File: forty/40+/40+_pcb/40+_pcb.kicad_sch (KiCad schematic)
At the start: 28 parts, among them J1 USB_C_Receptacle_USB2.0_16P, J2 Conn_01x02_Socket, SW1 Switch, U1 USB6B1, U2 USBLC6-2SC6, U3 nRF52840, U4 MCP73831-2-OT, Y2 Crystal_GND3

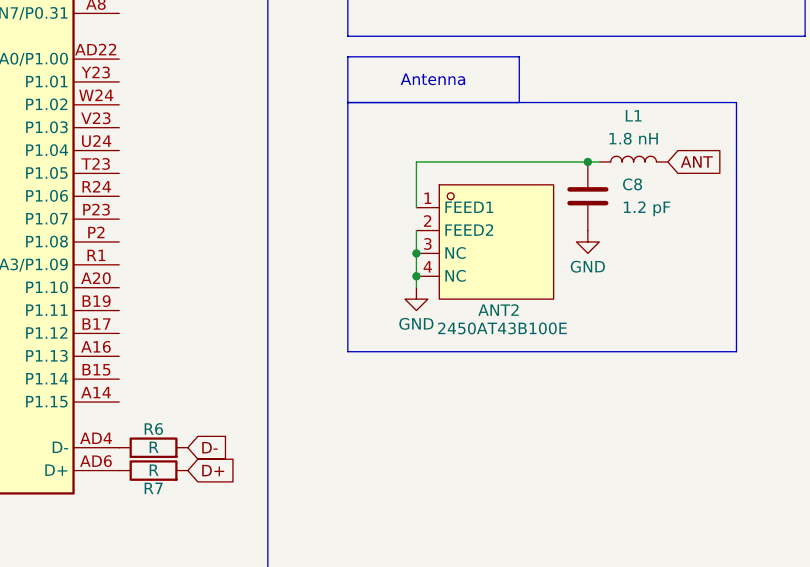
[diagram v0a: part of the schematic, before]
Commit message: Add EasyEDA to KiCad symbol and 3D models
Added EasyEDA to KiCad symbol library and associated 3D STEP/WRL models for capacitor and resistor. Updated 40+ PCB project files, removed autosave and lock files, and added a backup ZIP.
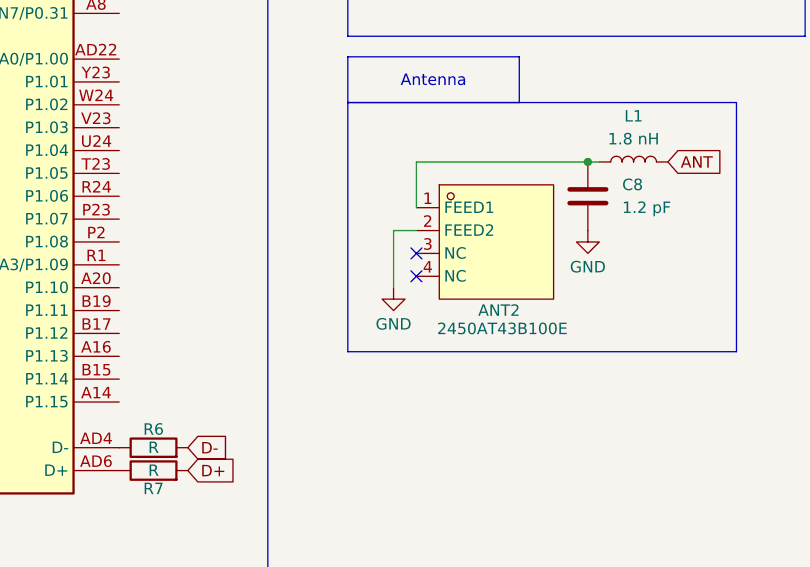
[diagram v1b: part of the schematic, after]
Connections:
- net GND: no longer ANT2.3 (NC), ANT2.4 (NC)
- no-connect marks 3 -> 5
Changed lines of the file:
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@@
-	)
-	(junction
-		(at 139.7 152.4)
-		(diameter 0)
-		(color 0 0 0 0)
 	)
 	(junction
@@
 	)
 	(junction
-		(at 139.7 154.94)
-		(diameter 0)
-		(color 0 0 0 0)
-	)
-	(junction
 		(at 213.36 142.24)
 		(diameter 0)
@@
 	)
 	(no_connect
+		(at 139.7 152.4)
+	)
+	(no_connect
 		(at 144.78 119.38)
+	)
+	(no_connect
+		(at 139.7 154.94)
 	)
 	(no_connect
@@
 	(wire
 		(pts
-			(xy 139.7 149.86) (xy 139.7 152.4)
-		)
-		(stroke
-			(width 0)
-			(type default)
-		)
-	)
-	(wire
-		(pts
 			(xy 223.52 127) (xy 231.14 127)
 		)
@@
 	(wire
 		(pts
+			(xy 137.16 149.86) (xy 139.7 149.86)
+		)
+		(stroke
+			(width 0)
+			(type default)
+		)
+	)
+	(wire
+		(pts
 			(xy 55.88 34.29) (xy 58.42 34.29)
 		)
@@
 	(wire
 		(pts
-			(xy 139.7 152.4) (xy 139.7 154.94)
-		)
-		(stroke
-			(width 0)
-			(type default)
-		)
-	)
-	(wire
-		(pts
 			(xy 38.1 153.67) (xy 38.1 156.21)
 		)
@@
 	(wire
 		(pts
-			(xy 139.7 154.94) (xy 139.7 156.21)
+			(xy 137.16 149.86) (xy 137.16 156.21)
 		)
 		(stroke
@@
 	(symbol
 		(lib_id "power:GND")
-		(at 139.7 156.21 0)
+		(at 137.16 156.21 0)
 		(unit 1)
 		(exclude_from_sim no)
@@
 		(dnp no)
 		(property "Reference" "#PWR019"
-			(at 139.7 162.56 0)
+			(at 137.16 162.56 0)
 			(effects
 				(font
@@
 		)
 		(property "Value" "GND"
-			(at 139.7 160.274 0)
+			(at 137.16 160.274 0)
 			(effects
 				(font
@@
 		)
 		(property "Footprint" ""
-			(at 139.7 156.21 0)
+			(at 137.16 156.21 0)
 			(effects
 				(font
@@
 		)
 		(property "Datasheet" ""
-			(at 139.7 156.21 0)
+			(at 137.16 156.21 0)
 			(effects
 				(font
@@
 		)
 		(property "Description" "Power symbol creates a global label with name \"GND\" , ground"
-			(at 139.7 156.21 0)
-			(effects
-				(font
+			(at 137.16 156.21 0)
+			(effects
+				(font

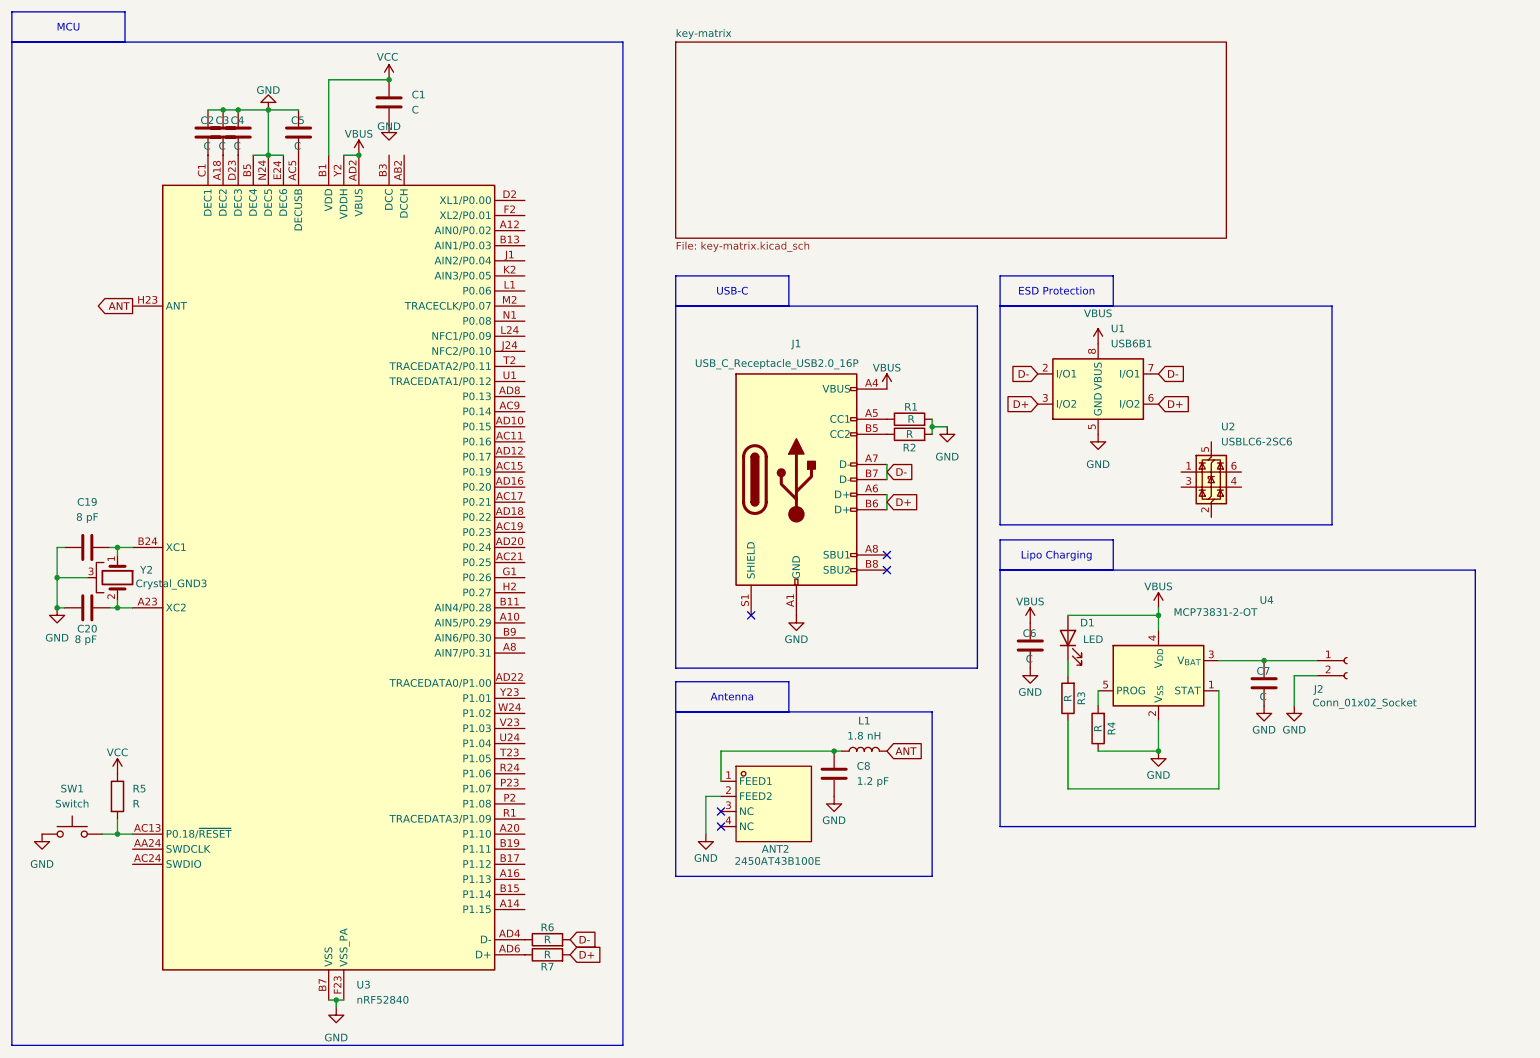
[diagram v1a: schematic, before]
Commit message: Add 40%+ keyboard layout and update PCB files
Added a new 40%+ keyboard layout JSON with function keys, updated and added KiCad PCB, schematic, and project files for the 40+ PCB, and included new backup and log files. Also added the nRF52840 spec sheet and made changes to the macropad PCB project file.
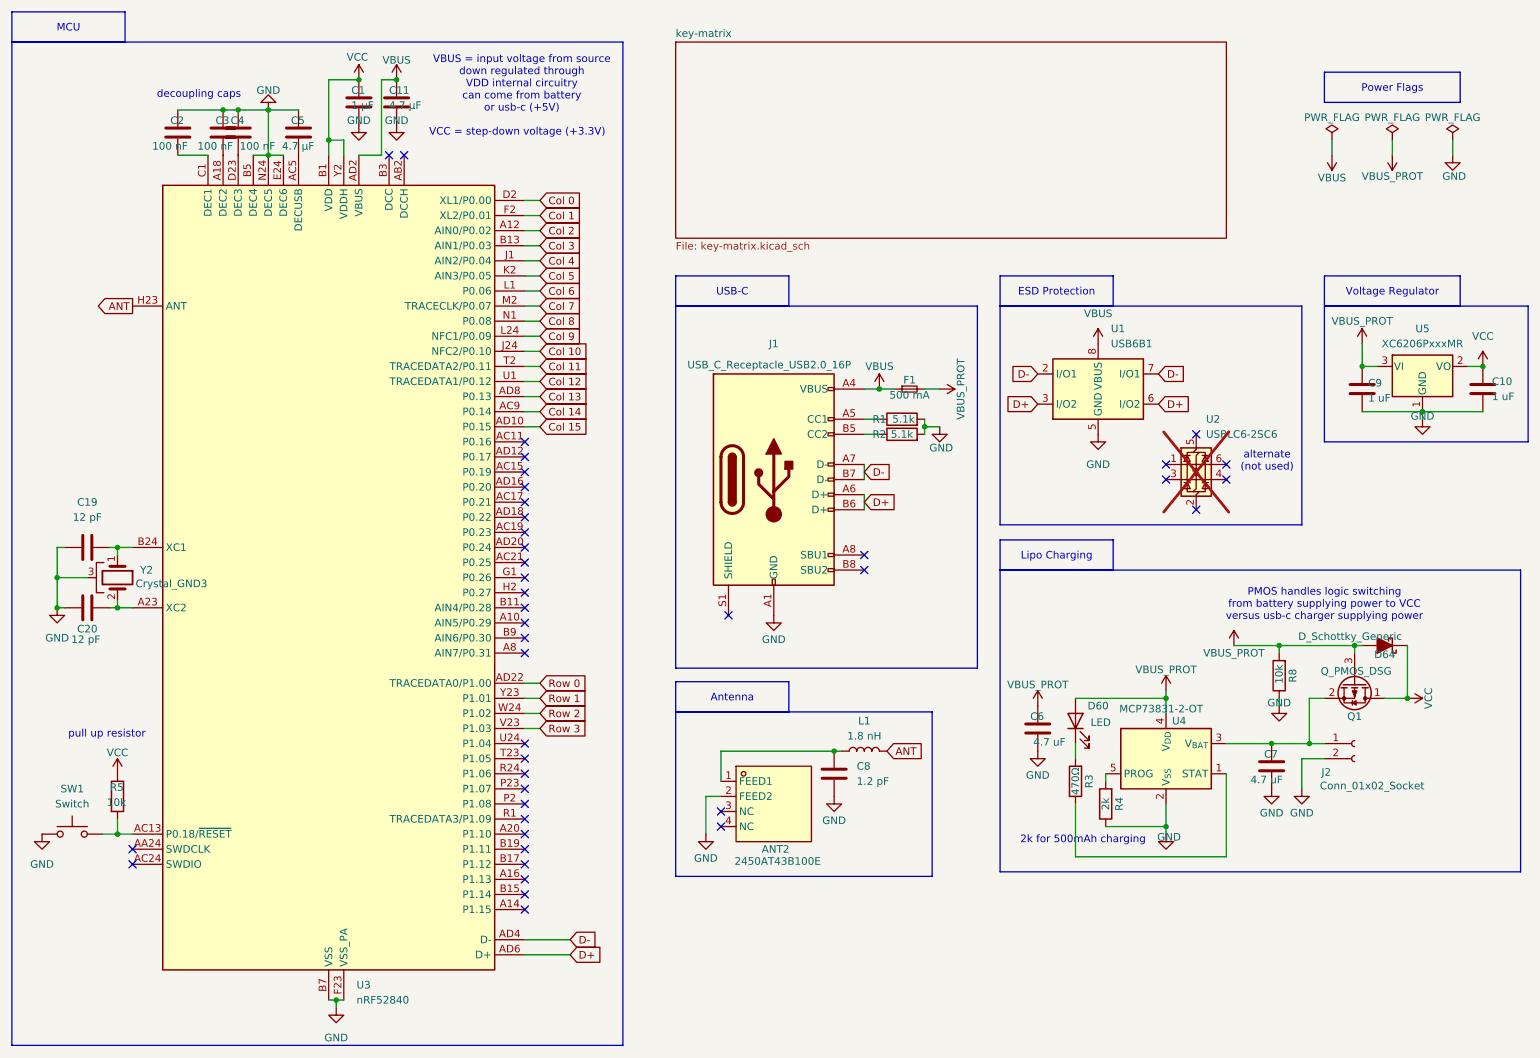
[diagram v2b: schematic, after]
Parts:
- removed R6, R7: R, symbol Device:R
- added C10, C9: 1 uF, Capacitor_SMD:C_0603_1608Metric_Pad1.08x0.95mm_HandSolder, symbol Device:C
- added C11: 4.7 µF, Capacitor_SMD:C_0603_1608Metric_Pad1.08x0.95mm_HandSolder, symbol Device:C
- added D64: D_Schottky_Generic, Diode_SMD:D_2114_3652Metric_Pad1.85x3.75mm_HandSolder, symbol PCM_Diode_Schottky_AKL:D_Schottky_Generic
- added F1: 500 mA, Fuse:Fuse_1206_3216Metric_Pad1.42x1.75mm_HandSolder, symbol Device:Fuse_Small
- added Q1: Q_PMOS_DSG, Package_TO_SOT_SMD:SOT-23, symbol Transistor_FET:Q_PMOS_DSG
- added R8: 10k, Resistor_SMD:R_0603_1608Metric_Pad0.98x0.95mm_HandSolder, symbol Device:R
- added U5: XC6206PxxxMR, Package_TO_SOT_SMD:SOT-23-3, symbol Regulator_Linear:XC6206PxxxMR
- C1: value C -> 1 µF; footprint (none) -> Capacitor_SMD:C_0603_1608Metric_Pad1.08x0.95mm_HandSolder
- C19, C20: value 8 pF -> 12 pF; footprint (none) -> Capacitor_SMD:C_0402_1005Metric_Pad0.74x0.62mm_HandSolder
- C2, C3, C4: value C -> 100 nF; footprint (none) -> Capacitor_SMD:C_0603_1608Metric_Pad1.08x0.95mm_HandSolder
- C5: value C -> 4.7 µF; footprint (none) -> Capacitor_SMD:C_0603_1608Metric_Pad1.08x0.95mm_HandSolder
- C6, C7: value C -> 4.7 uF; footprint (none) -> Capacitor_SMD:C_0603_1608Metric_Pad1.08x0.95mm_HandSolder
- C8: footprint (none) -> Capacitor_SMD:C_0402_1005Metric_Pad0.74x0.62mm_HandSolder
- D60: renamed from D1; footprint (none) -> LED_SMD:LED_0603_1608Metric_Pad1.05x0.95mm_HandSolder
- J1: footprint (none) -> Connector_USB:USB_C_Receptacle_HRO_TYPE-C-31-M-12
- J2: footprint (none) -> Connector_JST:JST_PH_S2B-PH-K_1x02_P2.00mm_Horizontal
- L1: footprint (none) -> Inductor_SMD:L_0402_1005Metric_Pad0.77x0.64mm_HandSolder
- R1, R2: value R -> 5.1k; footprint (none) -> Resistor_SMD:R_0603_1608Metric_Pad0.98x0.95mm_HandSolder
- R3: value R -> 470Ω; footprint (none) -> Resistor_SMD:R_0603_1608Metric_Pad0.98x0.95mm_HandSolder
- R4: value R -> 2k; footprint (none) -> Resistor_SMD:R_0603_1608Metric_Pad0.98x0.95mm_HandSolder
- R5: value R -> 10k; footprint (none) -> Resistor_SMD:R_0603_1608Metric_Pad0.98x0.95mm_HandSolder
- SW1: footprint Connector_JST:JST_EH_B2B-EH-A_1x02_P2.50mm_Vertical -> Button_Switch_SMD:SW_SPST_TL3342
- U2: now not fitted
- U4: footprint Package_TO_SOT_SMD:SOT-23-5 -> Package_TO_SOT_SMD:SOT-23-5_HandSoldering
- Y2: footprint (none) -> Crystal:Crystal_SMD_3225-4Pin_3.2x2.5mm_HandSoldering
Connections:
- net D+: now also U3.AD6 (D+)
- net D-: now also U3.AD4 (D-)
- net GND: now also C10.2, C11.2, C9.2, R8.1, U5.1 (GND)
- net VBUS: now also C11.1, F1.1; no longer C6.1, D60.2 (A), U3.Y2 (VDDH), U4.4 (V_{DD})
- net VCC: now also U3.Y2 (VDDH), C10.1, D64.1 (K), Q1.1 (D), U5.2 (VO)
- net at C7.1, J2.1 (Pin_1), U4.3 (V_{BAT}): now also Q1.2 (S)
- net Col 2: now reaches U3.A12 (AIN0/P0.02)
- net Col 14: now reaches U3.AC9 (P0.14)
- net Col 15: now reaches U3.AD10 (P0.15)
- net Row 0: now reaches U3.AD22 (TRACEDATA0/P1.00)
- net Col 13: now reaches U3.AD8 (P0.13)
- net Col 3: now reaches U3.B13 (AIN1/P0.03)
- net Col 0: now reaches U3.D2 (XL1/P0.00)
- net Col 1: now reaches U3.F2 (XL2/P0.01)
- net Col 4: now reaches U3.J1 (AIN2/P0.04)
- net Col 10: now reaches U3.J24 (NFC2/P0.10)
- net Col 5: now reaches U3.K2 (AIN3/P0.05)
- net Col 6: now reaches U3.L1 (P0.06)
- net Col 9: now reaches U3.L24 (NFC1/P0.09)
- net Col 7: now reaches U3.M2 (TRACECLK/P0.07)
- net Col 8: now reaches U3.N1 (P0.08)
- net Col 11: now reaches U3.T2 (TRACEDATA2/P0.11)
- net Col 12: now reaches U3.U1 (TRACEDATA1/P0.12)
- net Row 3: now reaches U3.V23 (P1.03)
- net Row 2: now reaches U3.W24 (P1.02)
- net Row 1: now reaches U3.Y23 (P1.01)
- new net VBUS_PROT: C6.1, C9.1, D60.2 (A), D64.2 (A), F1.2, Q1.3 (G), R8.2, U4.4 (V_{DD}), U5.3 (VI)
- no-connect marks 5 -> 42
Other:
- note added: "2k for 500mAh charging"
- note added: "PMOS handles logic switching from battery supplying power to VCC versus usb-c charger supplying power"
- note added: "VBUS = input voltage from source down regulated through VDD internal circuitry can come from battery or usb-c (+5V)"
- note added: "VCC = step-down voltage (+3.3V)"
- note added: "alternate (not used)"
- note added: "decoupling caps"
- note added: "pull up resistor"
- title: (none) -> 40% Keyboard with left side 2 column function cluster
- moved on the sheet: C1, C2, C6, C7, D60, J1, J2, R1, R2, R3, R4, U4
